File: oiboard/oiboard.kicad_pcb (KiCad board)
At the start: 2 copper layers, 99.1 x 99.1 mm, 52 parts, among them J1 Conn_01x04, J2 Conn_01x04, J3 Conn_01x04, J4 Conn_01x04, J5 Conn_01x04, J6 Conn_01x04, J7 SPI PORT, Q1 2N3904, Q2 2N3904, Q3 2N3904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

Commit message: finalize pcb design 0.0
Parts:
- removed TP1, TP2: TestPoint, TestPoint:TestPoint_THTPad_D1.5mm_Drill0.7mm
- added H1: MountingHole, MountingHole:MountingHole_3mm, F.Cu at (177.2, 132.1)
- added H2: MountingHole, MountingHole:MountingHole_3mm, F.Cu at (167.0, 91.4)
- added H3: MountingHole, MountingHole:MountingHole_3mm, F.Cu at (148.0, 92.7)
- added H4: MountingHole, MountingHole:MountingHole_3mm, F.Cu at (90.2, 97.8)
- moved R4 70.5 mm to (169.5, 131.4), turned to 180 degrees
- moved R8 65.5 mm to (160.0, 66.7)
- moved R2 65.4 mm to (101.6, 131.4)
- moved R6 57.8 mm to (102.2, 66.7)
- moved R3 25.2 mm to (149.2, 65.4), turned to -90 degrees
- moved Q3 17.8 mm to (157.5, 124.5)
- moved R5 14.9 mm to (137.8, 62.2), turned to 180 degrees
- moved SW1 13.1 mm to (119.4, 121.9), turned to 180 degrees
- moved U1 11.4 mm to (129.5, 74.3), turned to 90 degrees
- moved R7 11.3 mm to (140.3, 62.2), turned to 0 degrees
- moved R12 10.3 mm to (114.3, 126.4)
- moved Q2 7.68 mm to (160.0, 72.1)
- moved D18 7.65 mm to (167.6, 71.8)
- moved R1 7.43 mm to (124.5, 64.1), turned to -90 degrees
- moved D17 5.68 mm to (99.1, 121.9), turned to 180 degrees
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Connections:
- A1 pad 24: /sensor_b -> /sensor_c
- A1 pad 25: /sensor_c -> /sensor_d
- A1 pad 26: /sensor_d -> /sensor_b
- D1 pad 5: unconnected-(D1-Pad5) -> /led_clock 
- D1 pad 6: unconnected-(D1-Pad6) -> /led_data
- D8 pad 1: unconnected-(D8-Pad1) -> Net-(D8-Pad1)
- D8 pad 2: unconnected-(D8-Pad2) -> Net-(D8-Pad2)
- D9 pad 1: unconnected-(D9-Pad1) -> Net-(D8-Pad1)
- D9 pad 2: unconnected-(D9-Pad2) -> Net-(D8-Pad2)
- R1 pad 1: Net-(J1-Pad3) -> Net-(J2-Pad3)
- R2 pad 2: Net-(J1-Pad2) -> Net-(J2-Pad2)
- R3 pad 1: Net-(J2-Pad3) -> Net-(J4-Pad3)
- R4 pad 1: Net-(J2-Pad2) -> Net-(J4-Pad2)
- R5 pad 1: Net-(J3-Pad3) -> Net-(J1-Pad3)
- R6 pad 1: Net-(J3-Pad2) -> Net-(J1-Pad2)
- R7 pad 1: Net-(J4-Pad3) -> Net-(J3-Pad3)
- R8 pad 1: Net-(J4-Pad2) -> Net-(J3-Pad2)
- U1 pad 12: Net-(J4-Pad2) -> Net-(J1-Pad2)
- U1 pad 13: Net-(J4-Pad3) -> Net-(J1-Pad3)
- U1 pad 14: /sensor_d -> /sensor_c
- U1 pad 2: Net-(J1-Pad3) -> Net-(J2-Pad3)
- U1 pad 3: Net-(J1-Pad2) -> Net-(J2-Pad2)
- U1 pad 5: Net-(J2-Pad2) -> Net-(J4-Pad2)
- U1 pad 6: Net-(J2-Pad3) -> Net-(J4-Pad3)
- U1 pad 8: /sensor_c -> /sensor_d
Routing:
- net +5V: track 0.00 -> 623.3 mm, vias 0 -> 14
- net Net-(J2-Pad2): track 0.00 -> 113.7 mm, vias 0 -> 1
- net /led_clock : track 0.00 -> 109.3 mm, vias 0 -> 1
- net /led_data: track 0.00 -> 106.7 mm, vias 0 -> 1
- net Net-(J2-Pad3): track 0.00 -> 103.3 mm, vias 0 -> 1
- net Net-(J4-Pad3): track 0.00 -> 86.0 mm
- net Net-(A1-Pad15): track 0.00 -> 84.7 mm, vias 0 -> 1
- net Net-(J4-Pad2): track 0.00 -> 84.3 mm, vias 0 -> 4
- net Net-(A1-Pad16): track 0.00 -> 81.1 mm, vias 0 -> 1
- net Net-(A1-Pad14): track 0.00 -> 80.6 mm, vias 0 -> 1
- net Net-(A1-Pad13): track 0.00 -> 77.0 mm, vias 0 -> 1
- net /led_c: track 0.00 -> 73.0 mm, vias 0 -> 1
- net /led_b: track 0.00 -> 61.5 mm, vias 0 -> 1
- net /sensor_d: track 0.00 -> 59.7 mm
- net /sensor_c: track 0.00 -> 57.6 mm, vias 0 -> 2
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- added copper zone on B.Cu, net GND
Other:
- board text added: "OIBOARD April 2022"
- board text added: "nabulator.com"
- board text added: "v 0.0"

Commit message: add logo to board
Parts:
- added G***: LOGO, DUMB:arrow_graphic, B.Cu at (159.4, 103.5)

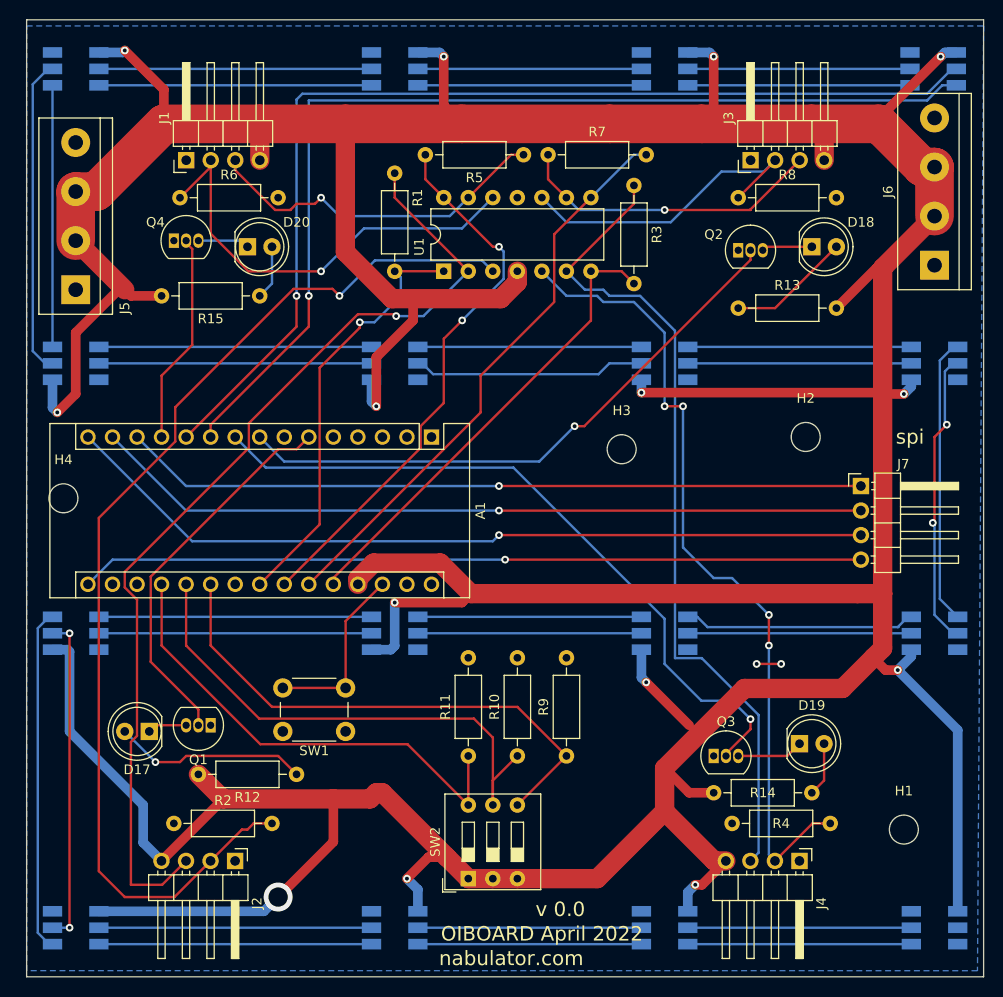
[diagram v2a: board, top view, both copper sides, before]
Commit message: add additional labels to the daughter oiboard
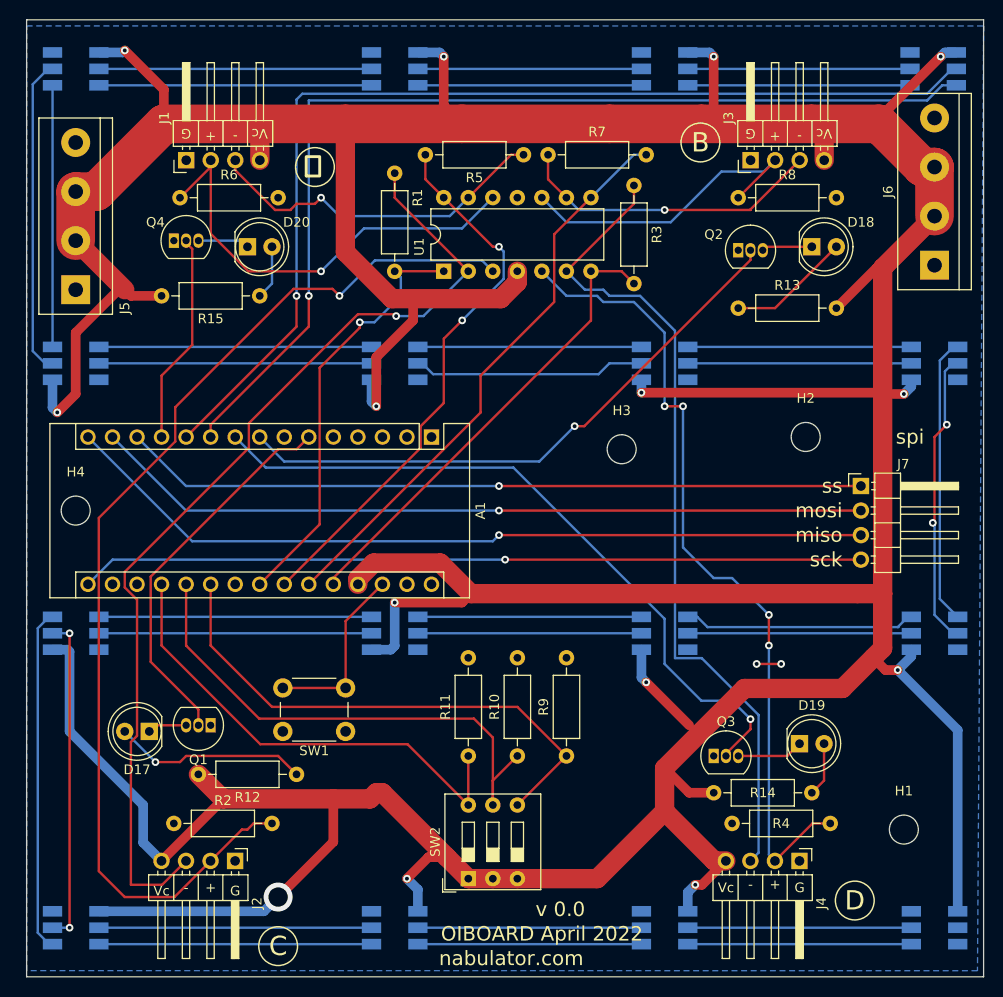
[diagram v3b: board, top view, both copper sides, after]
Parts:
- moved H4 1.80 mm to (91.4, 99.1)
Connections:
- net Net-(A1-Pad13) renamed /SS
- net Net-(A1-Pad14) renamed /MOSI
- net Net-(A1-Pad15) renamed /MISO
- net Net-(A1-Pad16) renamed /SCK
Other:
- board text added: "+"
- board text added: "-"
- board text added: "B"
- board text added: "C"
- board text added: "D"
- board text added: "G"
- board text added: "Vc"
- board text added: "led_clock"
- board text added: "led_data"
- board text added: "miso"
- board text added: "mosi"
- board text added: "sck"
- board text added: "ss"
- board text added: "あ"
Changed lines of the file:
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@@
   (net 11 "/led_clock ")
   (net 12 "/led_d")
-  (net 13 "Net-(A1-Pad13)")
-  (net 14 "Net-(A1-Pad14)")
-  (net 15 "Net-(A1-Pad15)")
-  (net 16 "Net-(A1-Pad16)")
+  (net 13 "/SS")
+  (net 14 "/MOSI")
+  (net 15 "/MISO")
+  (net 16 "/SCK")
   (net 17 "unconnected-(A1-Pad17)")
   (net 18 "unconnected-(A1-Pad18)")
@@
   )
   (footprint "MountingHole:MountingHole_3mm" (layer "F.Cu")
-    (at 90.17 97.79)
+    (at 91.44 99.06)
     (descr "Mounting Hole 3mm, no annular")
     (tags "mounting hole 3mm no annular")
@@
     (fp_line (start 10.04 -0.32) (end 10.04 0.32) (layer "F.Fab") (width 0.1))
     (pad "1" thru_hole rect (at 0 0) (size 1.7 1.7) (drill 1) (layers *.Cu *.Mask)
-      (net 13 "Net-(A1-Pad13)") (pinfunction "Pin_1") (pintype "passive"))
+      (net 13 "/SS") (pinfunction "Pin_1") (pintype "passive"))
     (pad "2" thru_hole oval (at 0 2.54) (size 1.7 1.7) (drill 1) (layers *.Cu *.Mask)
-      (net 14 "Net-(A1-Pad14)") (pinfunction "Pin_2") (pintype "passive"))
+      (net 14 "/MOSI") (pinfunction "Pin_2") (pintype "passive"))
     (pad "3" thru_hole oval (at 0 5.08) (size 1.7 1.7) (drill 1) (layers *.Cu *.Mask)
-      (net 15 "Net-(A1-Pad15)") (pinfunction "Pin_3") (pintype "passive"))
+      (net 15 "/MISO") (pinfunction "Pin_3") (pintype "passive"))
     (pad "4" thru_hole oval (at 0 7.62) (size 1.7 1.7) (drill 1) (layers *.Cu *.Mask)
-      (net 16 "Net-(A1-Pad16)") (pinfunction "Pin_4") (pintype "passive"))
+      (net 16 "/SCK") (pinfunction "Pin_4") (pintype "passive"))
     (model "${KICAD6_3DMODEL_DIR}/Connector_PinHeader_2.54mm.3dshapes/PinHeader_1x04_P2.54mm_Horizontal.wrl"
       (offset (xyz 0 0 0))
@@
       (net 12 "/led_d") (pinfunction "D9") (pintype "bidirectional"))
     (pad "13" thru_hole oval (at 0 30.48 270) (size 1.6 1.6) (drill 1) (layers *.Cu *.Mask)
-      (net 13 "Net-(A1-Pad13)") (pinfunction "D10") (pintype "bidirectional"))
+      (net 13 "/SS") (pinfunction "D10") (pintype "bidirectional"))
     (pad "14" thru_hole oval (at 0 33.02 270) (size 1.6 1.6) (drill 1) (layers *.Cu *.Mask)
-      (net 14 "Net-(A1-Pad14)") (pinfunction "D11") (pintype "bidirectional"))
+      (net 14 "/MOSI") (pinfunction "D11") (pintype "bidirectional"))
     (pad "15" thru_hole oval (at 0 35.56 270) (size 1.6 1.6) (drill 1) (layers *.Cu *.Mask)
-      (net 15 "Net-(A1-Pad15)") (pinfunction "D12") (pintype "bidirectional"))
+      (net 15 "/MISO") (pinfunction "D12") (pintype "bidirectional"))
     (pad "16" thru_hole oval (at 15.24 35.56 270) (size 1.6 1.6) (drill 1) (layers *.Cu *.Mask)
-      (net 16 "Net-(A1-Pad16)") (pinfunction "D13") (pintype "bidirectional"))
+      (net 16 "/SCK") (pinfunction "D13") (pintype "bidirectional"))
     (pad "17" thru_hole oval (at 15.24 33.02 270) (size 1.6 1.6) (drill 1) (layers *.Cu *.Mask)
       (net 17 "unconnected-(A1-Pad17)") (pinfunction "3V3") (pintype "power_out+no_connect"))
@@
     )
   )
+  (gr_circle (center 112.395 144.145) (end 113.03 142.24) (layer "F.SilkS") (width 0.15) (fill none))
+  (gr_circle (center 172.085 139.425) (end 172.72 137.52) (layer "F.SilkS") (width 0.15) (fill none))
+  (gr_circle (center 156.106954 60.96) (end 156.741954 59.055) (layer "F.SilkS") (width 0.15) (fill none))
+  (gr_circle (center 116.205 63.5) (end 116.84 61.595) (layer "F.SilkS") (width 0.15) (fill none))
   (gr_rect (start 86.36 48.26) (end 185.42 147.32) (layer "Edge.Cuts") (width 0.1) (fill none))
+  (gr_text "led_clock\n" (at 114.3 77.47 90) (layer "B.SilkS")
+    (effects (font (size 1 1) (thickness 0.15)) (justify left mirror))
+  )
+  (gr_text "led_data" (at 115.57 77.47 90) (layer "B.SilkS")
+    (effects (font (size 1 1) (thickness 0.15)) (justify left mirror))
+  )
+  (gr_text "-\n" (at 102.87 138.095) (layer "F.SilkS")
+    (effects (font (size 1 1) (thickness 0.1)))
+  )
+  (gr_text "D\n" (at 172.085 139.425) (layer "F.SilkS")
+    (effects (font (size 2 2) (thickness 0.5)))
+  )
   (gr_text "OIBOARD April 2022" (at 139.7 142.875) (layer "F.SilkS")
     (effects (font (size 1.5 1.5) (thickness 0.3)))
   )
+  (gr_text "Vc" (at 158.75 138.095) (layer "F.SilkS")
+    (effects (font (size 1 1) (thickness 0.1)))
+  )
+  (gr_text "mosi" (at 170.815 99.06) (layer "F.SilkS")
+    (effects (font (size 1.5 1.5) (thickness 0.3)) (justify right))
+  )
+  (gr_text "-\n" (at 161.29 137.76) (layer "F.SilkS")
+    (effects (font (size 1 1) (thickness 0.1)))
+  )
   (gr_text "spi" (at 177.8 91.44) (layer "F.SilkS")
     (effects (font (size 1.5 1.5) (thickness 0.3)))
   )
+  (gr_text "+" (at 163.83 137.76) (layer "F.SilkS")
+    (effects (font (size 1 1) (thickness 0.1)))
+  )
+  (gr_text "sck\n" (at 170.815 104.14) (layer "F.SilkS")
+    (effects (font (size 1.5 1.5) (thickness 0.3)) (justify right))
+  )
+  (gr_text "Vc" (at 110.49 60.025 180) (layer "F.SilkS")
+    (effects (font (size 1 1) (thickness 0.1)))
+  )
+  (gr_text "あ\n" (at 116 63.5) (layer "F.SilkS")
+    (effects (font (size 2 2) (thickness 0.3)))
+  )
+  (gr_text "G" (at 161.29 60.025 180) (layer "F.SilkS")
+    (effects (font (size 1 1) (thickness 0.1)))
+  )
+  (gr_text "Vc" (at 168.91 60.025 180) (layer "F.SilkS")
+    (effects (font (size 1 1) (thickness 0.1)))
+  )
   (gr_text "nabulator.com" (at 136.525 145.415) (layer "F.SilkS")
     (effects (font (size 1.5 1.5) (thickness 0.3)))
   )
+  (gr_text "B\n" (at 156.106954 60.96) (layer "F.SilkS")
+    (effects (font (size 2 2) (thickness 0.5)))
+  )
+  (gr_text "G" (at 102.87 60.025 180) (layer "F.SilkS")
+    (effects (font (size 1 1) (thickness 0.1)))
+  )
+  (gr_text "+" (at 163.83 60.36 180) (layer "F.SilkS")
+    (effects (font (size 1 1) (thickness 0.1)))
+  )
+  (gr_text "G" (at 166.37 138.095) (layer "F.SilkS")
+    (effects (font (size 1 1) (thickness 0.1)))
+  )
+  (gr_text "C\n" (at 112.395 144.145) (layer "F.SilkS")
+    (effects (font (size 2 2) (thickness 0.5)))
+  )
+  (gr_text "+" (at 105.41 60.36 180) (layer "F.SilkS")
+    (effects (font (size 1 1) (thickness 0.1)))
+  )
+  (gr_text "ss" (at 170.815 96.52) (layer "F.SilkS")
+    (effects (font (size 1.5 1.5) (thickness 0.3)) (justify right))
+  )
+  (gr_text "miso" (at 170.815 101.6) (layer "F.SilkS")
+    (effects (font (size 1.5 1.5) (thickness 0.3)) (justify right))
+  )
+  (gr_text "Vc" (at 100.33 138.43) (layer "F.SilkS")
+    (effects (font (size 1 1) (thickness 0.1)))
+  )
+  (gr_text "-\n" (at 166.37 60.36 180) (layer "F.SilkS")
+    (effects (font (size 1 1) (thickness 0.1)))
+  )
+  (gr_text "-\n" (at 107.95 60.36 180) (layer "F.SilkS")
+    (effects (font (size 1 1) (thickness 0.1)))
+  )
+  (gr_text "+" (at 105.41 138.095) (layer "F.SilkS")
+    (effects (font (size 1 1) (thickness 0.1)))
+  )
   (gr_text "v 0.0\n" (at 141.605 140.335) (layer "F.SilkS")
     (effects (font (size 1.5 1.5) (thickness 0.3)))
   )
+  (gr_text "G" (at 107.95 138.43) (layer "F.SilkS")
+    (effects (font (size 1 1) (thickness 0.1)))
+  )
   (segment (start 129.54 57.15) (end 131.420489 59.030489) (width 1) (layer "F.Cu") (net 4))
   (segment (start 119.355489 59.030489) (end 131.420489 59.030489) (width 4) (layer "F.Cu") (net 4))
@@
     )
   )
+  (group "" (id 6a78f426-b0f1-4a10-8b9d-203792afdc98)
+    (members
+      10f5f92a-8126-4c3a-9e81-4d232773605b
+      6452138c-3310-48c8-b90c-7c5735e80a97
+    )
+  )
+  (group "" (id bb5bd5af-89d5-46f6-bfc1-d483c802f61a)
+    (members
+      6c3acabf-9323-4fb0-a9fe-d35f688d3616
+      f8d8c4c5-899f-4bae-9aee-5b1fd3a230bf
+    )
+  )
+  (group "" (id e9435f9d-96e0-471c-86be-70a565e44442)
+    (members
+      57e1ad96-958c-49e5-939b-f83b30219ead
+      a227cbde-5623-43a9-91d7-71aa1535d1da
+    )
+  )
